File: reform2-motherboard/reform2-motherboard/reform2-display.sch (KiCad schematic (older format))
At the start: 1 part

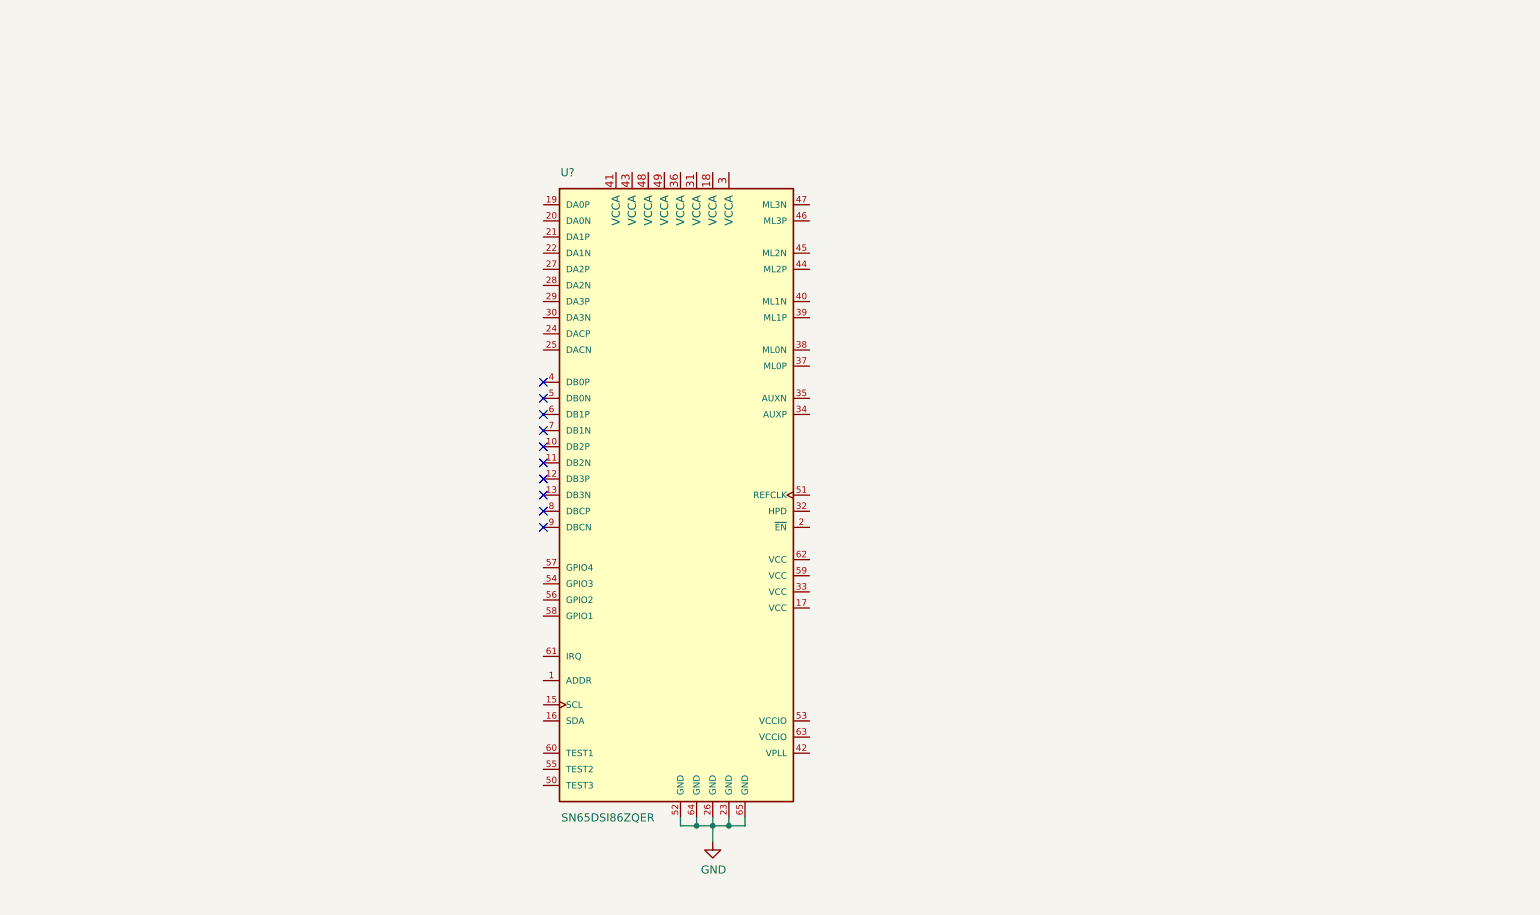
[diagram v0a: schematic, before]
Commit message: reform2: schematic work, mainly power, display, first footprint tests
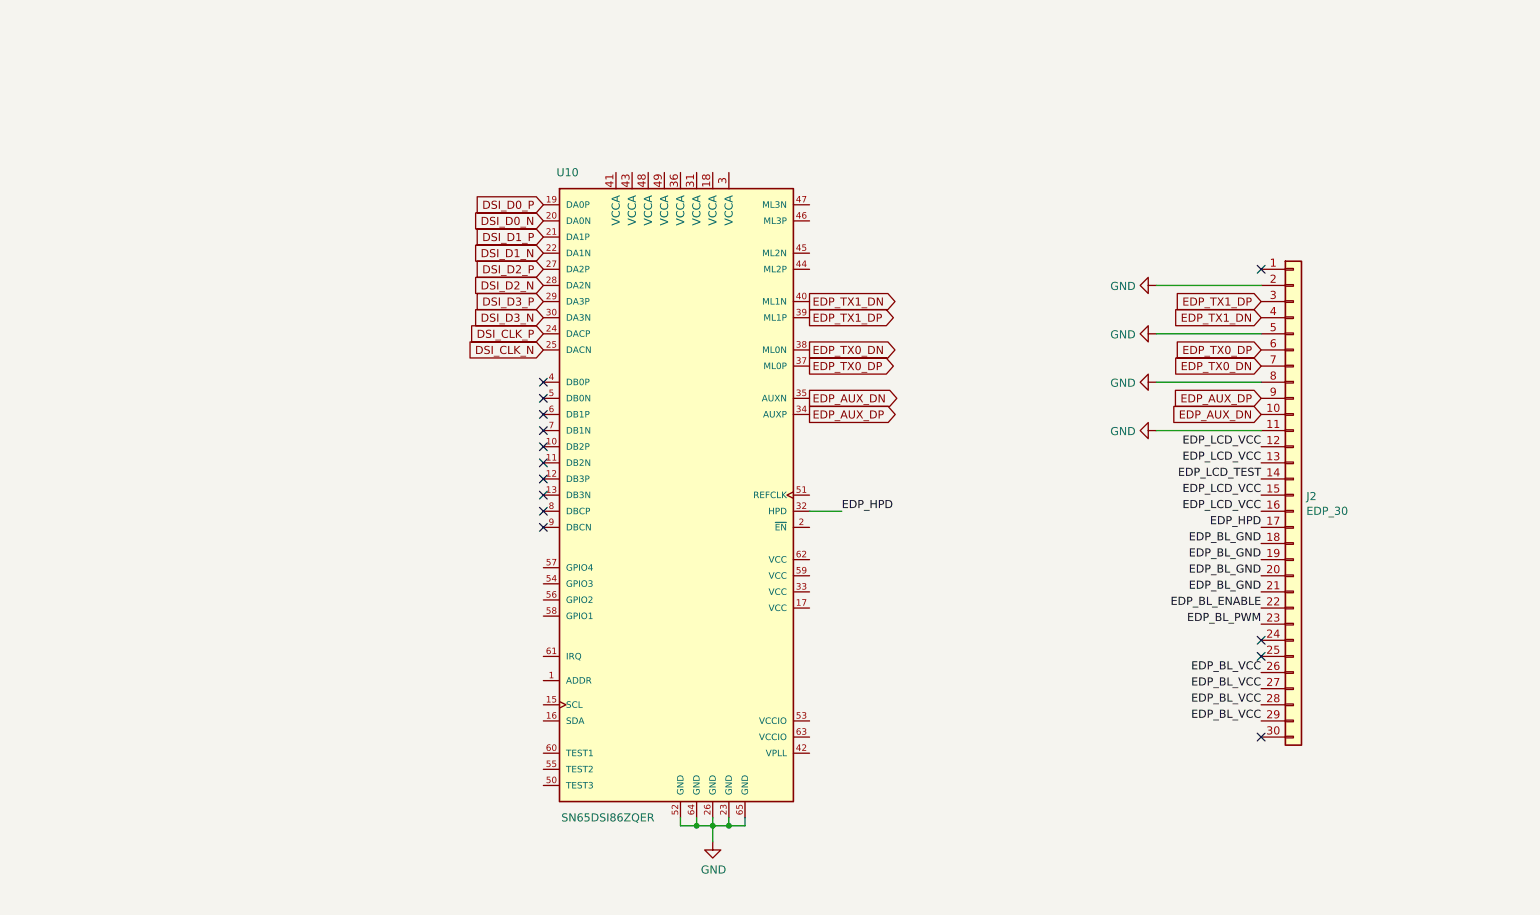
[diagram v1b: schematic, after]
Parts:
- added J2: EDP_30, Connector_FFC-FPC:Hirose_FH12-30S-0.5SH_1x30-1MP_P0.50mm_Horizontal, symbol Connector_Generic:Conn_01x30
- U10: renamed from U?; footprint BGA64C50P9X9_500X500X100 -> Package_QFP:HTQFP-64-1EP_10x10mm_P0.5mm_EP8x8mm
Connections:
- net GND: now also J2.11 (Pin_11), J2.2 (Pin_2), J2.5 (Pin_5), J2.8 (Pin_8)
- net DSI_D0_P: now reaches U10.19 (DA0P)
- net DSI_D0_N: now reaches U10.20 (DA0N)
- net DSI_D1_P: now reaches U10.21 (DA1P)
- net DSI_D1_N: now reaches U10.22 (DA1N)
- net DSI_CLK_P: now reaches U10.24 (DACP)
- net DSI_CLK_N: now reaches U10.25 (DACN)
- net DSI_D2_P: now reaches U10.27 (DA2P)
- net DSI_D2_N: now reaches U10.28 (DA2N)
- net DSI_D3_P: now reaches U10.29 (DA3P)
- net DSI_D3_N: now reaches U10.30 (DA3N)
- net EDP_HPD: now reaches U10.32 (HPD)
- net EDP_HPD: now also J2.17 (Pin_17)
- net EDP_AUX_DP: now reaches U10.34 (AUXP)
- net EDP_AUX_DP: now also J2.9 (Pin_9)
- net EDP_AUX_DN: now reaches U10.35 (AUXN)
- net EDP_AUX_DN: now also J2.10 (Pin_10)
- net EDP_TX0_DP: now reaches U10.37 (ML0P)
- net EDP_TX0_DP: now also J2.6 (Pin_6)
- net EDP_TX0_DN: now reaches U10.38 (ML0N)
- net EDP_TX0_DN: now also J2.7 (Pin_7)
- net EDP_TX1_DP: now reaches U10.39 (ML1P)
- net EDP_TX1_DP: now also J2.3 (Pin_3)
- net EDP_TX1_DN: now reaches U10.40 (ML1N)
- net EDP_TX1_DN: now also J2.4 (Pin_4)
- new net EDP_BL_ENABLE: J2.22 (Pin_22)
- new net EDP_BL_GND: J2.18 (Pin_18), J2.19 (Pin_19), J2.20 (Pin_20), J2.21 (Pin_21)
- new net EDP_BL_PWM: J2.23 (Pin_23)
- new net EDP_BL_VCC: J2.26 (Pin_26), J2.27 (Pin_27), J2.28 (Pin_28), J2.29 (Pin_29)
- new net EDP_LCD_TEST: J2.14 (Pin_14)
- new net EDP_LCD_VCC: J2.12 (Pin_12), J2.13 (Pin_13), J2.15 (Pin_15), J2.16 (Pin_16)
- no-connect marks 10 -> 14
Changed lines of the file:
@@
 $EndDescr
 $Comp
-L reform2:SN65DSI86ZQER U?
+L reform2:SN65DSI86ZQER U10
 U 1 1 5D1D2542
 P 4950 3450
-F 0 "U?" H 4400 5250 50  0000 C CNN
+F 0 "U10" H 4400 5250 50  0000 C CNN
 F 1 "SN65DSI86ZQER" H 4650 1250 50  0000 C CNN
-F 2 "BGA64C50P9X9_500X500X100" H 4400 800 50  0001 L BNN
+F 2 "Package_QFP:HTQFP-64-1EP_10x10mm_P0.5mm_EP8x8mm" H 4400 800 50  0001 L BNN
 F 3 "" H 4950 3450 50  0001 L BNN
 F 4 "Dual-Channel MIPI® DSI to Embedded DisplayPort™ _eDP _ Bridge 64-BGA MICROSTAR JUNIOR -40 to 85" H 2850 950 50  0001 L BNN "Field4"
@@
 $EndComp
 $Comp
-L power:GND #PWR?
+L power:GND #PWR0146
 U 1 1 5D1D45E5
 P 5300 5800
-F 0 "#PWR?" H 5300 5550 50  0001 C CNN
+F 0 "#PWR0146" H 5300 5550 50  0001 C CNN
 F 1 "GND" H 5305 5627 50  0000 C CNN
 F 2 "" H 5300 5800 50  0001 C CNN
@@
 NoConn ~ 4250 3750
 NoConn ~ 4250 3850
+Text GLabel 4250 2550 0    50   Input ~ 0
+DSI_D3_N
+Text GLabel 4250 2450 0    50   Input ~ 0
+DSI_D3_P
+Text GLabel 4250 1950 0    50   Input ~ 0
+DSI_D0_N
+Text GLabel 4250 1850 0    50   Input ~ 0
+DSI_D0_P
+Text GLabel 4250 2750 0    50   Input ~ 0
+DSI_CLK_N
+Text GLabel 4250 2650 0    50   Input ~ 0
+DSI_CLK_P
+Text GLabel 4250 2150 0    50   Input ~ 0
+DSI_D1_N
+Text GLabel 4250 2050 0    50   Input ~ 0
+DSI_D1_P
+Text GLabel 4250 2250 0    50   Input ~ 0
+DSI_D2_P
+Text GLabel 4250 2350 0    50   Input ~ 0
+DSI_D2_N
+$Comp
+L Connector_Generic:Conn_01x30 J2
+U 1 1 5DA8371C
+P 8900 3650
+F 0 "J2" H 8980 3642 50  0000 L CNN
+F 1 "EDP_30" H 8980 3551 50  0000 L CNN
+F 2 "Connector_FFC-FPC:Hirose_FH12-30S-0.5SH_1x30-1MP_P0.50mm_Horizontal" H 8900 3650 50  0001 C CNN
+F 3 "~" H 8900 3650 50  0001 C CNN
+	1    8900 3650
+	1    0    0    -1
+$EndComp
+Text GLabel 8700 2750 0    50   Input ~ 0
+EDP_TX0_DP
+Text GLabel 8700 2850 0    50   Input ~ 0
+EDP_TX0_DN
+Text GLabel 8700 2450 0    50   Input ~ 0
+EDP_TX1_DP
+Text GLabel 8700 2550 0    50   Input ~ 0
+EDP_TX1_DN
+Text GLabel 8700 3050 0    50   Input ~ 0
+EDP_AUX_DP
+Text GLabel 8700 3150 0    50   Input ~ 0
+EDP_AUX_DN
+Text Label 8700 3350 2    50   ~ 0
+EDP_LCD_VCC
+Text Label 8700 3450 2    50   ~ 0
+EDP_LCD_VCC
+Text Label 8700 3650 2    50   ~ 0
+EDP_LCD_VCC
+Text Label 8700 3750 2    50   ~ 0
+EDP_LCD_VCC
+Text Label 8700 3850 2    50   ~ 0
+EDP_HPD
+Text Label 8700 3950 2    50   ~ 0
+EDP_BL_GND
+Text Label 8700 4050 2    50   ~ 0
+EDP_BL_GND
+Text Label 8700 4150 2    50   ~ 0
+EDP_BL_GND
+Text Label 8700 4250 2    50   ~ 0
+EDP_BL_GND
+Text Label 8700 4350 2    50   ~ 0
+EDP_BL_ENABLE
+Text Label 8700 4450 2    50   ~ 0
+EDP_BL_PWM
+NoConn ~ 8700 4550
+NoConn ~ 8700 4650
+NoConn ~ 8700 5150
+Text Label 8700 4750 2    50   ~ 0
+EDP_BL_VCC
+Text Label 8700 4850 2    50   ~ 0
+EDP_BL_VCC
+Text Label 8700 4950 2    50   ~ 0
+EDP_BL_VCC
+Text Label 8700 5050 2    50   ~ 0
+EDP_BL_VCC
+Text Label 8700 3550 2    50   ~ 0
+EDP_LCD_TEST
+$Comp
+L power:GND #PWR0147
+U 1 1 5DA89FD9
+P 8050 3250
+F 0 "#PWR0147" H 8050 3000 50  0001 C CNN
+F 1 "GND" V 8055 3122 50  0000 R CNN
+F 2 "" H 8050 3250 50  0001 C CNN
+F 3 "" H 8050 3250 50  0001 C CNN
+	1    8050 3250
+	0    1    1    0
+$EndComp
+Wire Wire Line
+	8050 3250 8700 3250
+$Comp
+L power:GND #PWR0148
+U 1 1 5DA8A3CC
+P 8050 2950
+F 0 "#PWR0148" H 8050 2700 50  0001 C CNN
+F 1 "GND" V 8055 2822 50  0000 R CNN
+F 2 "" H 8050 2950 50  0001 C CNN
+F 3 "" H 8050 2950 50  0001 C CNN
+	1    8050 2950
+	0    1    1    0
+$EndComp
+$Comp
+L power:GND #PWR0149
+U 1 1 5DA8A5CE
+P 8050 2650
+F 0 "#PWR0149" H 8050 2400 50  0001 C CNN
+F 1 "GND" V 8055 2522 50  0000 R CNN
+F 2 "" H 8050 2650 50  0001 C CNN
+F 3 "" H 8050 2650 50  0001 C CNN
+	1    8050 2650
+	0    1    1    0
+$EndComp
+$Comp
+L power:GND #PWR0150
+U 1 1 5DA8A7A0
+P 8050 2350
+F 0 "#PWR0150" H 8050 2100 50  0001 C CNN
+F 1 "GND" V 8055 2222 50  0000 R CNN
+F 2 "" H 8050 2350 50  0001 C CNN
+F 3 "" H 8050 2350 50  0001 C CNN
+	1    8050 2350
+	0    1    1    0
+$EndComp
+NoConn ~ 8700 2250
+Wire Wire Line
+	8050 2350 8700 2350
+Wire Wire Line
+	8700 2650 8050 2650
+Wire Wire Line
+	8050 2950 8700 2950
+Text GLabel 5900 2550 2    50   Output ~ 0
+EDP_TX1_DP
+Text GLabel 5900 2450 2    50   Output ~ 0
+EDP_TX1_DN
+Text GLabel 5900 2850 2    50   Output ~ 0
+EDP_TX0_DP
+Text GLabel 5900 2750 2    50   Output ~ 0
+EDP_TX0_DN
+Text GLabel 5900 3150 2    50   Output ~ 0
+EDP_AUX_DP
+Text GLabel 5900 3050 2    50   Output ~ 0
+EDP_AUX_DN
+Text Label 6100 3750 0    50   ~ 0
+EDP_HPD
+Wire Wire Line
+	6100 3750 5900 3750
 $EndSCHEMATC

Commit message: WIP reform2: more schematics ground work on USB, PCIe, Display, Audio, Power
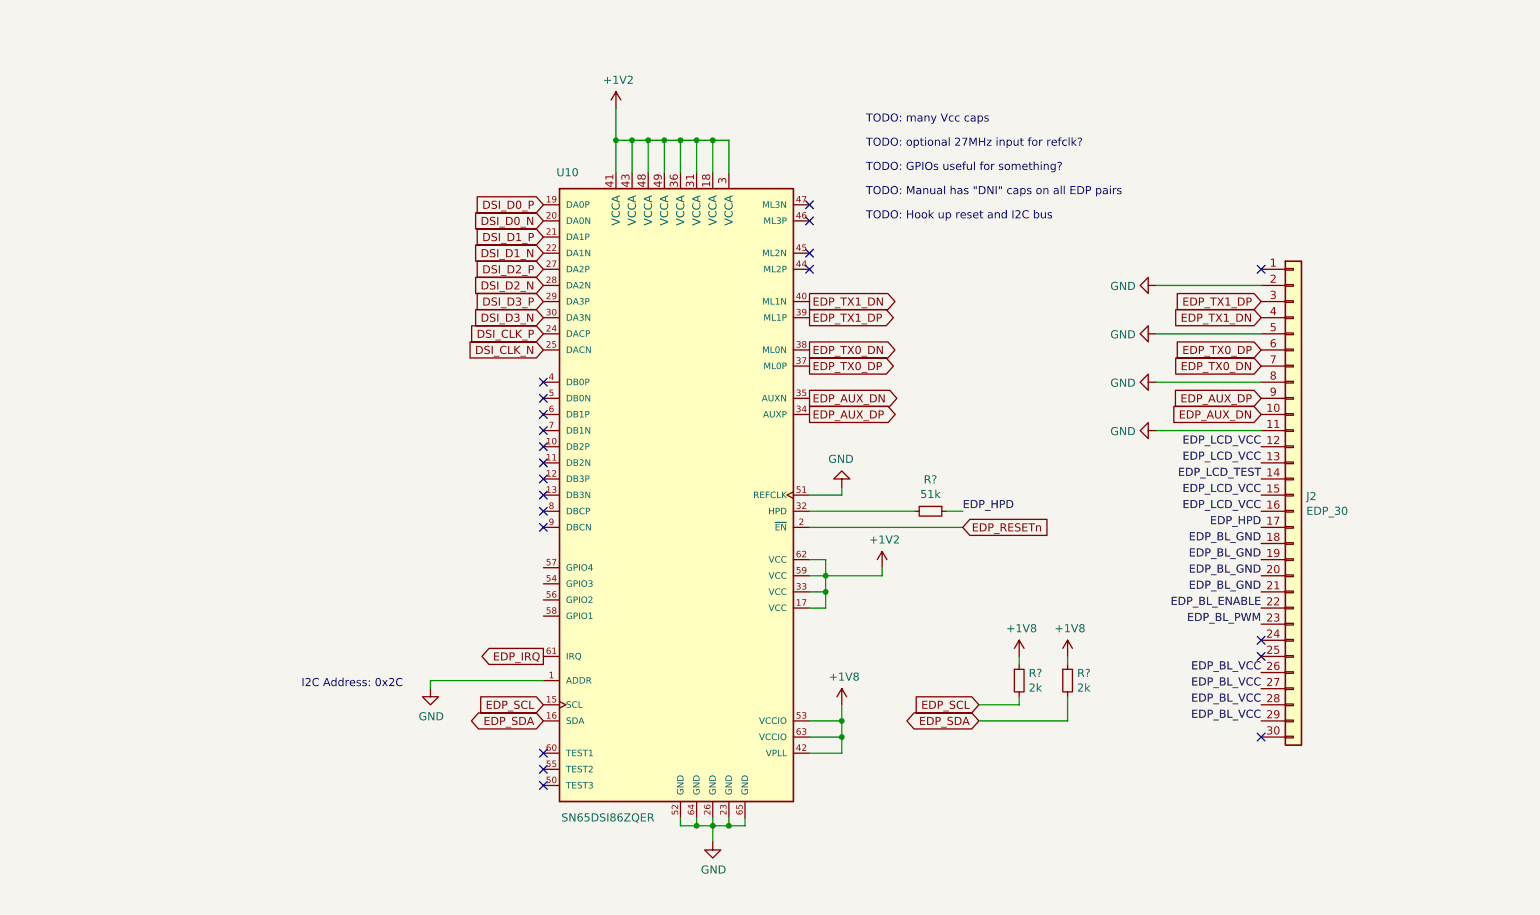
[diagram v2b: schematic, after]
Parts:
- added R?: 51k, symbol Device:R_Small
- added R? (x2): 2k, symbol Device:R_Small
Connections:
- net EDP_HPD: now also R?.1; no longer U10.32 (HPD)
- net GND: now also U10.1 (ADDR), U10.51 (REFCLK)
- net EDP_SCL: now reaches U10.15 (SCL)
- net EDP_SCL: now also R?.2
- net EDP_SDA: now reaches U10.16 (SDA)
- net EDP_SDA: now also R?.2
- net +1V2: now reaches U10.17 (VCC)
- net +1V2: now also U10.18 (VCCA), U10.3 (VCCA), U10.31 (VCCA), U10.33 (VCC), U10.36 (VCCA), U10.41 (VCCA), U10.43 (VCCA), U10.48 (VCCA), U10.49 (VCCA), U10.59 (VCC), U10.62 (VCC)
- net EDP_RESETn: now reaches U10.2 (~EN~)
- net +1V8: now reaches U10.42 (VPLL)
- net +1V8: now also U10.53 (VCCIO), U10.63 (VCCIO), R?.1, R?.1
- net EDP_IRQ: now reaches U10.61 (IRQ)
- new net: R?.2, U10.32 (HPD)
- no-connect marks 14 -> 21
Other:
- note added: "I2C Address: 0x2C"
- note added: "TODO: GPIOs useful for something?"
- note added: "TODO: Hook up reset and I2C bus"
- note added: "TODO: Manual has "DNI" caps on all EDP pairs"
- note added: "TODO: many Vcc caps"
- note added: "TODO: optional 27MHz input for refclk?"

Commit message: WIP reform2: more power/charger details in schematic, footprint fixes
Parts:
- R64, R65, R66: renamed from R?; footprint (none) -> Resistor_SMD:R_0603_1608Metric
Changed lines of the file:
@@
 TODO: many Vcc caps
 $Comp
-L power:+1V2 #PWR?
+L power:+1V2 #PWR037
 U 1 1 5DA8B6EB
 P 4700 1250
-F 0 "#PWR?" H 4700 1100 50  0001 C CNN
+F 0 "#PWR037" H 4700 1100 50  0001 C CNN
 F 1 "+1V2" H 4715 1423 50  0000 C CNN
 F 2 "" H 4700 1250 50  0001 C CNN
@@
 	5300 1450 5400 1450
 $Comp
-L power:+1V2 #PWR?
+L power:+1V2 #PWR040
 U 1 1 5DA8EE88
 P 6350 4100
-F 0 "#PWR?" H 6350 3950 50  0001 C CNN
+F 0 "#PWR040" H 6350 3950 50  0001 C CNN
 F 1 "+1V2" H 6365 4273 50  0000 C CNN
 F 2 "" H 6350 4100 50  0001 C CNN
@@
 	6350 4150 6000 4150
 $Comp
-L power:+1V8 #PWR?
+L power:+1V8 #PWR039
 U 1 1 5DA98038
 P 6100 4950
-F 0 "#PWR?" H 6100 4800 50  0001 C CNN
+F 0 "#PWR039" H 6100 4800 50  0001 C CNN
 F 1 "+1V8" H 6115 5123 50  0000 C CNN
 F 2 "" H 6100 4950 50  0001 C CNN
@@
 NoConn ~ 4250 5250
 $Comp
-L Device:R_Small R?
+L Device:R_Small R64
 U 1 1 5DAA503E
 P 6650 3750
-F 0 "R?" V 6454 3750 50  0000 C CNN
+F 0 "R64" V 6454 3750 50  0000 C CNN
 F 1 "51k" V 6545 3750 50  0000 C CNN
-F 2 "" H 6650 3750 50  0001 C CNN
+F 2 "Resistor_SMD:R_0603_1608Metric" H 6650 3750 50  0001 C CNN
 F 3 "~" H 6650 3750 50  0001 C CNN
 	1    6650 3750
@@
 	6750 3750 6850 3750
 $Comp
-L power:GND #PWR?
+L power:GND #PWR038
 U 1 1 5DAA7616
 P 6100 3600
-F 0 "#PWR?" H 6100 3350 50  0001 C CNN
+F 0 "#PWR038" H 6100 3350 50  0001 C CNN
 F 1 "GND" H 6105 3427 50  0000 C CNN
 F 2 "" H 6100 3600 50  0001 C CNN
@@
 EDP_IRQ
 $Comp
-L power:GND #PWR?
+L power:GND #PWR036
 U 1 1 5DAABCBB
 P 3550 4850
-F 0 "#PWR?" H 3550 4600 50  0001 C CNN
+F 0 "#PWR036" H 3550 4600 50  0001 C CNN
 F 1 "GND" H 3555 4677 50  0000 C CNN
 F 2 "" H 3550 4850 50  0001 C CNN
@@
 EDP_SDA
 $Comp
-L power:+1V8 #PWR?
+L power:+1V8 #PWR041
 U 1 1 5DAB54EA
 P 7200 4650
-F 0 "#PWR?" H 7200 4500 50  0001 C CNN
+F 0 "#PWR041" H 7200 4500 50  0001 C CNN
 F 1 "+1V8" H 7215 4823 50  0000 C CNN
 F 2 "" H 7200 4650 50  0001 C CNN
@@
 $EndComp
 $Comp
-L Device:R_Small R?
+L Device:R_Small R65
 U 1 1 5DAB5CC1
 P 7200 4800
-F 0 "R?" H 7259 4846 50  0000 L CNN
+F 0 "R65" H 7259 4846 50  0000 L CNN
 F 1 "2k" H 7259 4755 50  0000 L CNN
-F 2 "" H 7200 4800 50  0001 C CNN
+F 2 "Resistor_SMD:R_0603_1608Metric" H 7200 4800 50  0001 C CNN
 F 3 "~" H 7200 4800 50  0001 C CNN
 	1    7200 4800
@@
 	7200 4950 7200 4900
 $Comp
-L Device:R_Small R?
+L Device:R_Small R66
 U 1 1 5DAB7962
 P 7500 4800
-F 0 "R?" H 7559 4846 50  0000 L CNN
+F 0 "R66" H 7559 4846 50  0000 L CNN
 F 1 "2k" H 7559 4755 50  0000 L CNN
-F 2 "" H 7500 4800 50  0001 C CNN
+F 2 "Resistor_SMD:R_0603_1608Metric" H 7500 4800 50  0001 C CNN
 F 3 "~" H 7500 4800 50  0001 C CNN
 	1    7500 4800
@@
 $EndComp
 $Comp
-L power:+1V8 #PWR?
+L power:+1V8 #PWR042
 U 1 1 5DAB7B54
 P 7500 4650
-F 0 "#PWR?" H 7500 4500 50  0001 C CNN
+F 0 "#PWR042" H 7500 4500 50  0001 C CNN
 F 1 "+1V8" H 7515 4823 50  0000 C CNN
 F 2 "" H 7500 4650 50  0001 C CNN
